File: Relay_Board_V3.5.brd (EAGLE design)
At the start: 160 x 100 mm, 65 parts

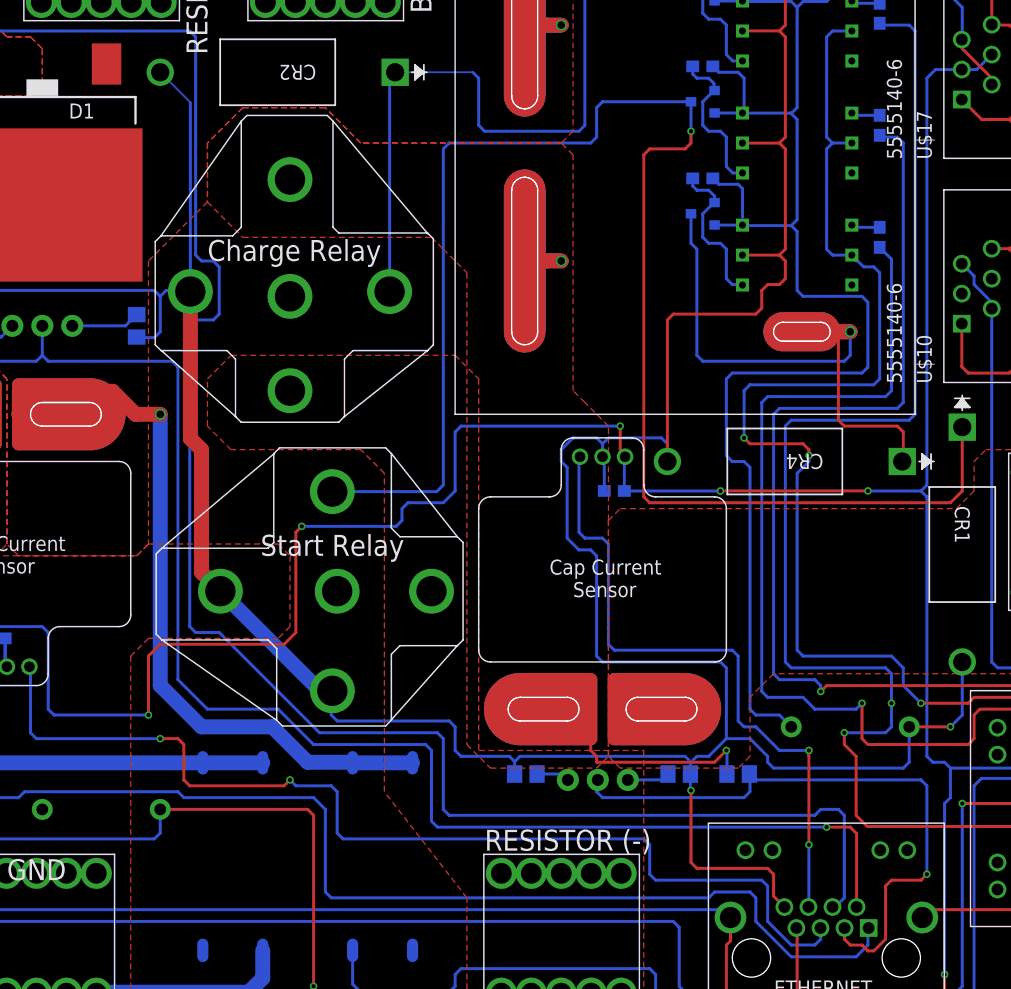
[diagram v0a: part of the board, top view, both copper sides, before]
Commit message: Fixed Traced Separation
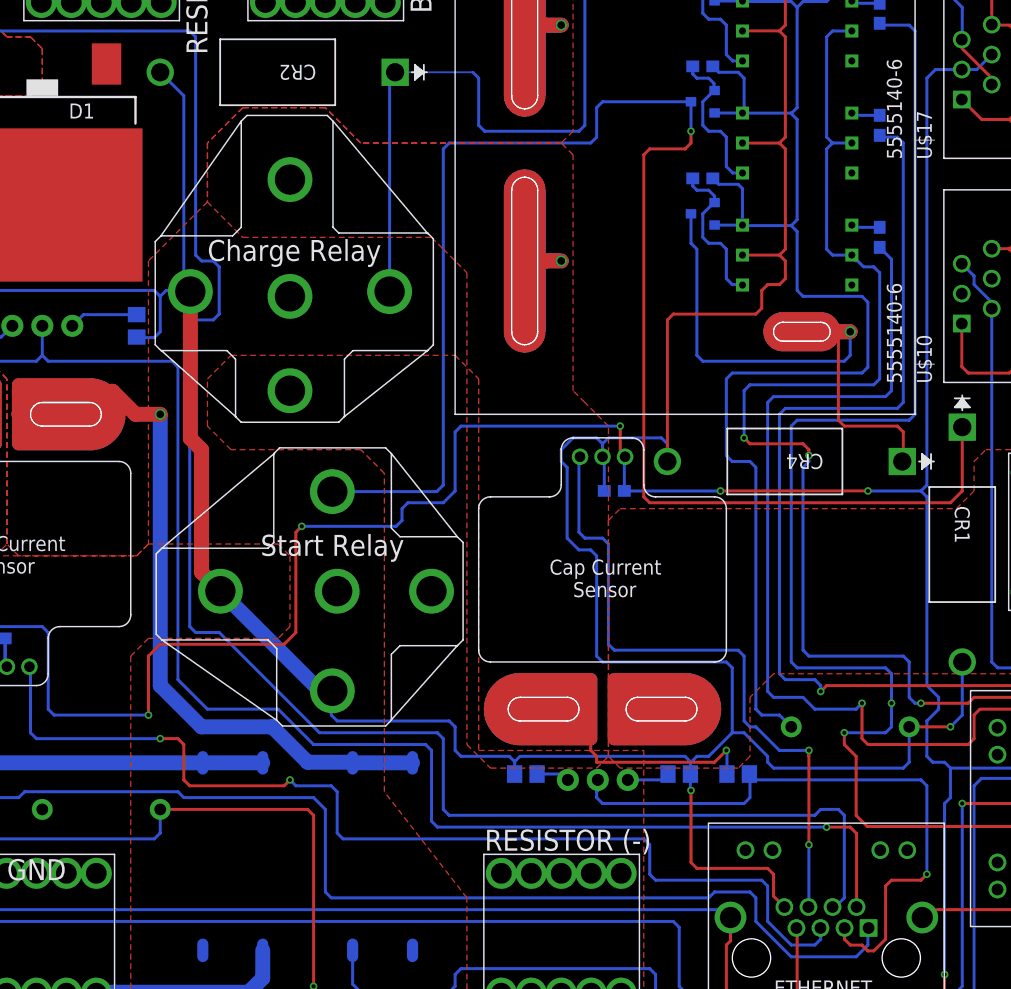
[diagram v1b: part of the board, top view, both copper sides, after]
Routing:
- net START_R: track 107.6 -> 106.6 mm
- net CHARGE_R: track 110.0 -> 109.0 mm
- net CAP_VOLT: track 52.6 -> 53.6 mm
- net CAP_R: track 90.6 -> 89.6 mm
- net 5V: track 279.1 -> 279.9 mm
